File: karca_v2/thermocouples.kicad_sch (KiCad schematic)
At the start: 11 parts, among them J8 Screw_Terminal_01x08, U14 NUP4202, U15 NUP4202, U16 NUP4202, U17 TLV9304xD

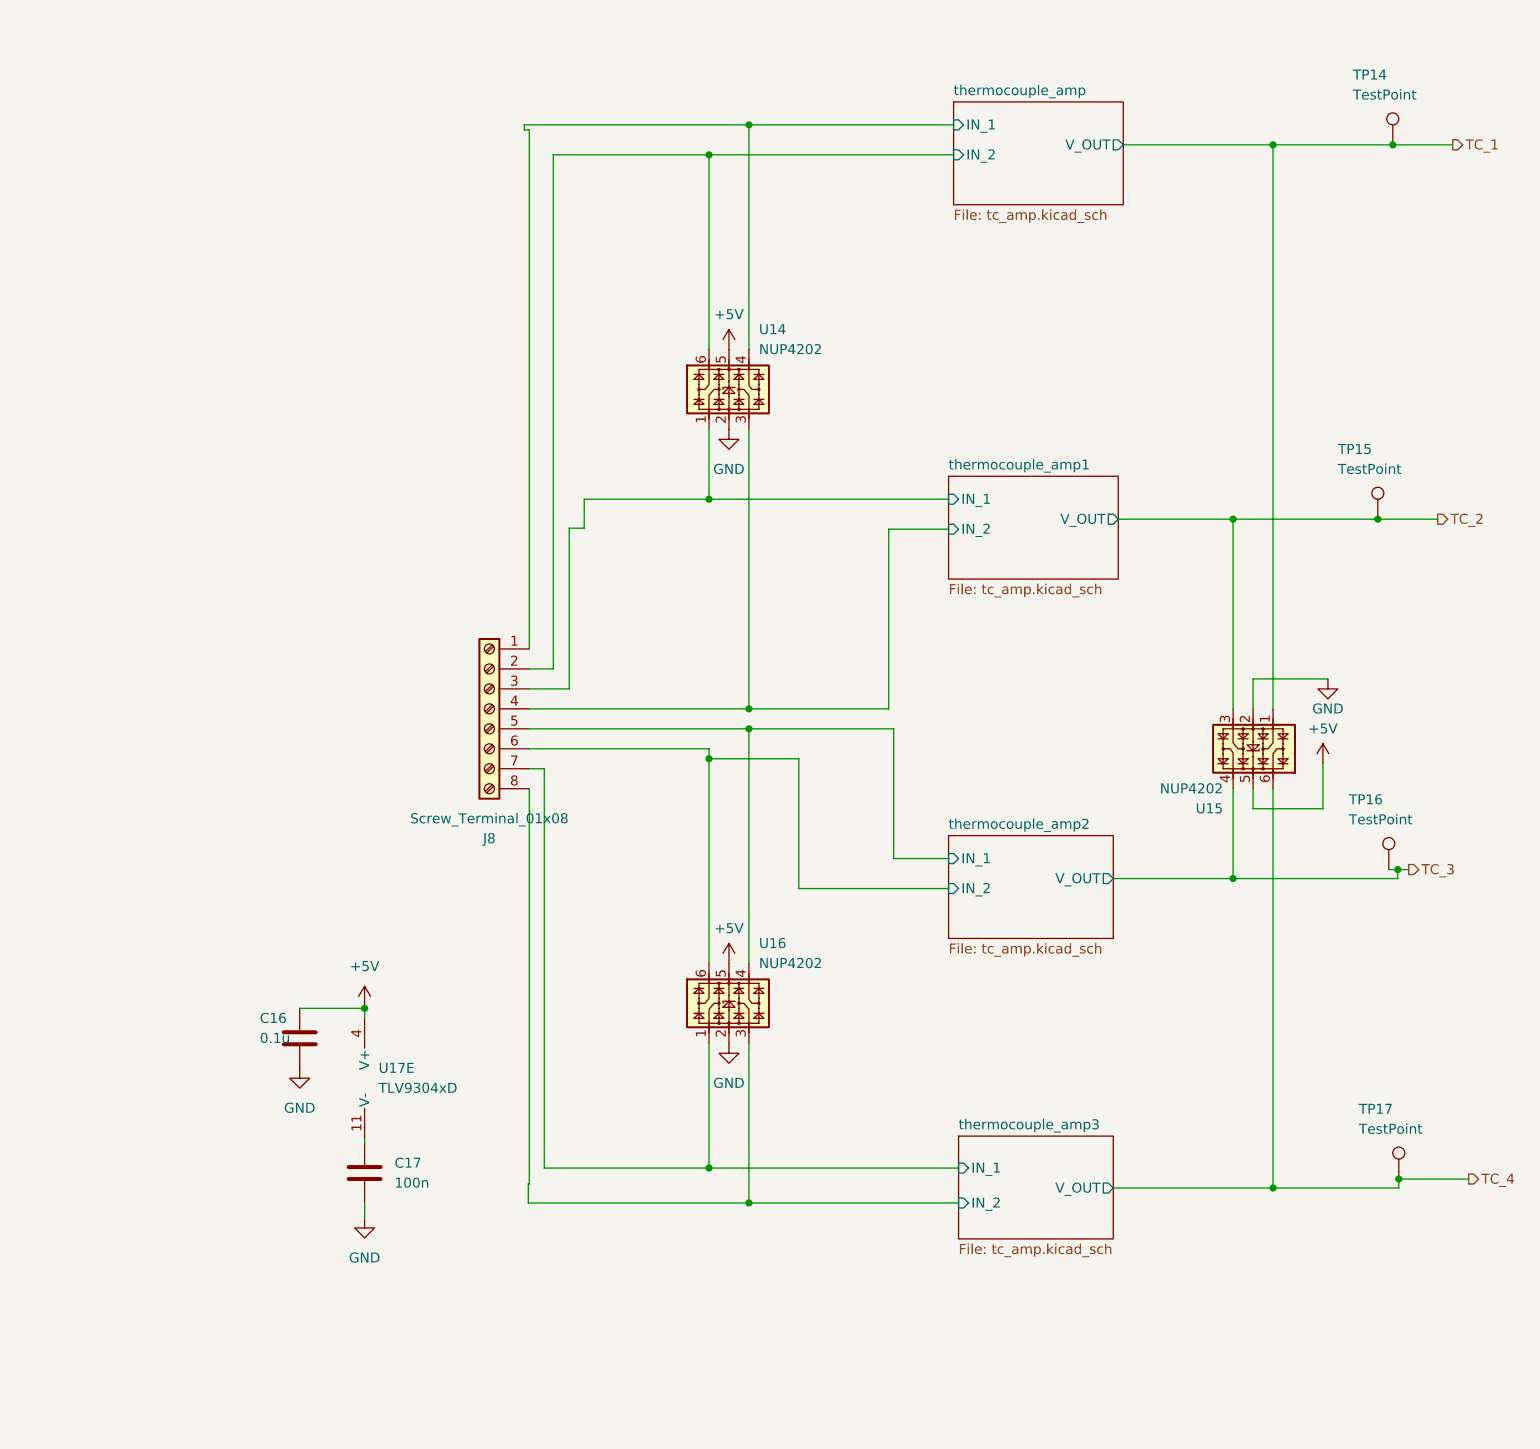
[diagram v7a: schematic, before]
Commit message: cleaned up documentation. Added production files and BOM. Marked Thermocouple components and THT components as DNP (excluded them from BOM too) to match version sent to JLCPCB for fabrication
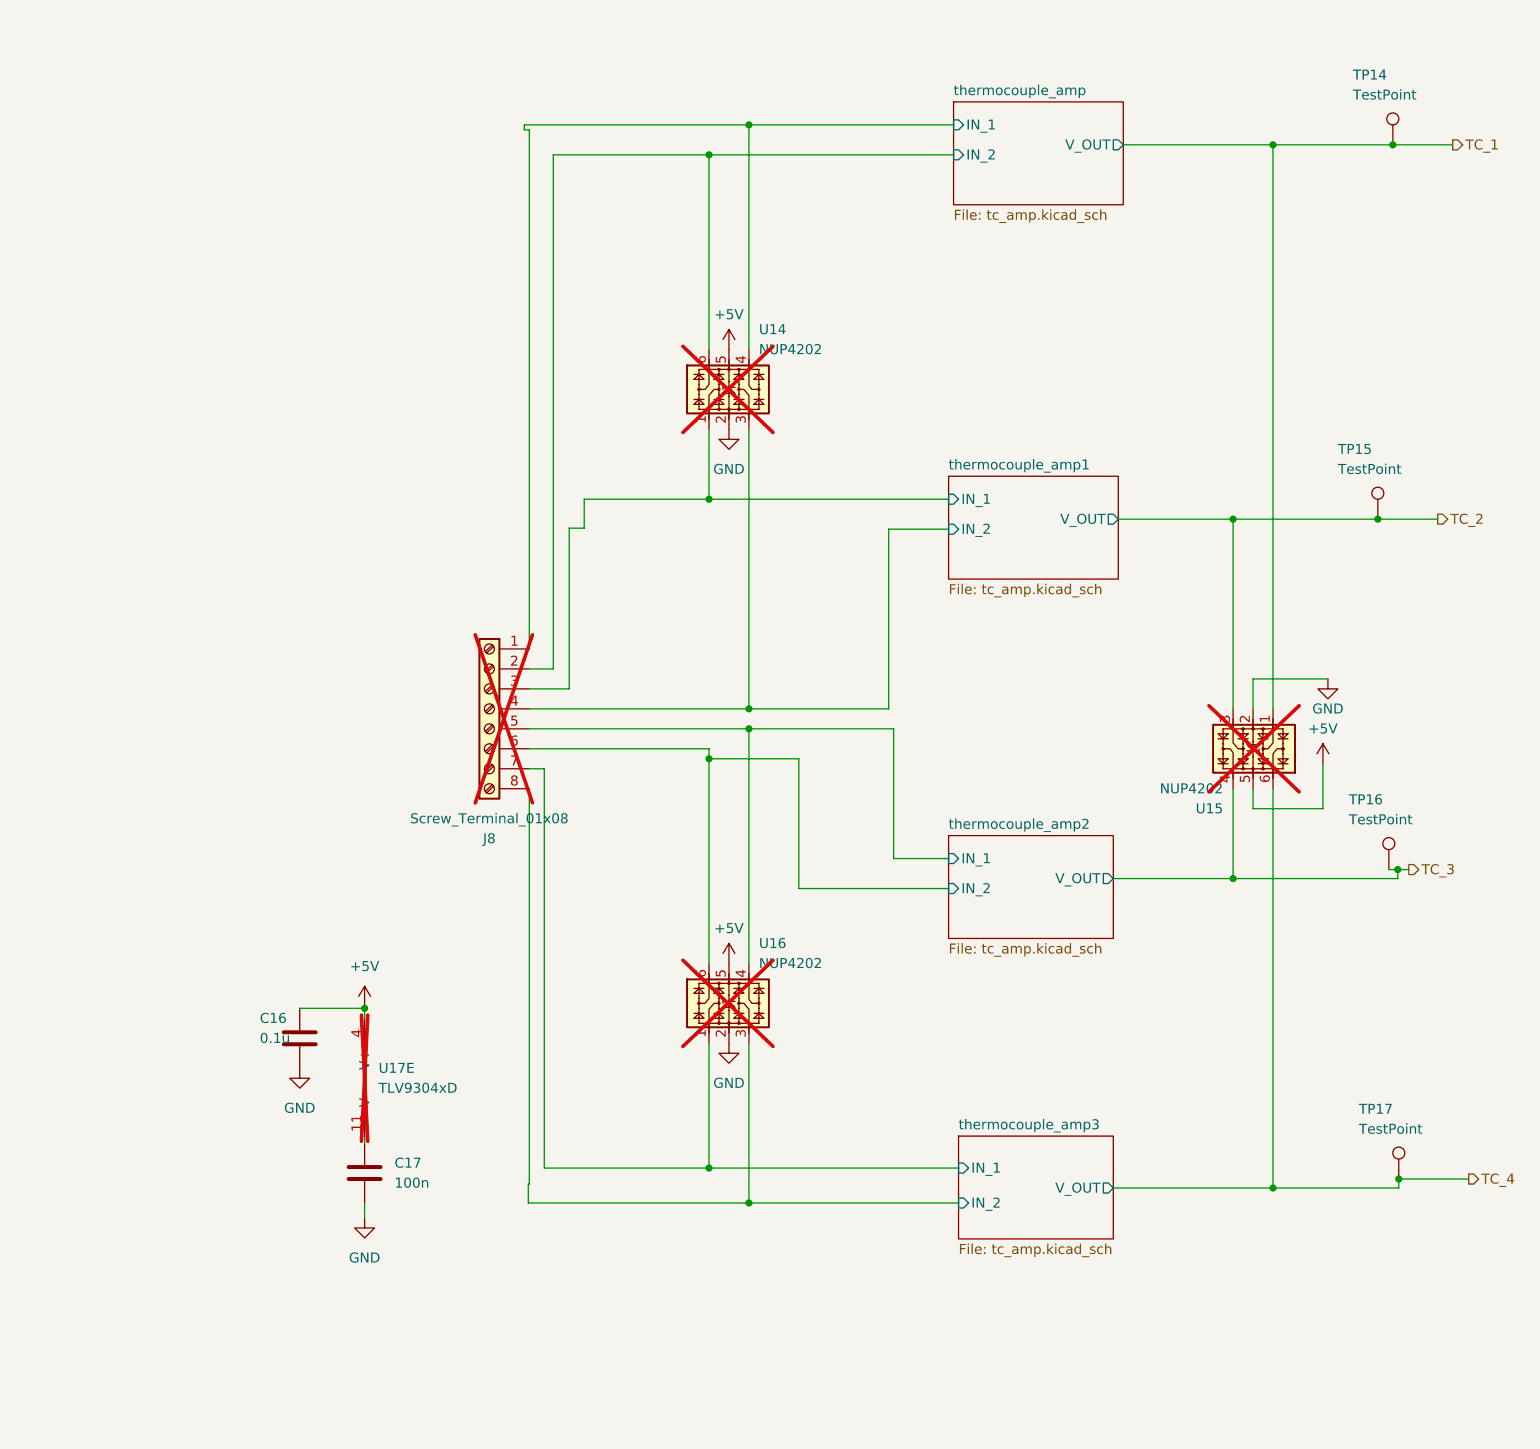
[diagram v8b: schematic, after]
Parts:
- J8, U14, U15, U16, U17: now not fitted; now left out of the parts list
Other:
- company: (none) -> Rice Eclipse
- title: (none) -> kARCA 2.0 Engine Control System
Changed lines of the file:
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@@
 (kicad_sch (version 20230121) (generator eeschema)
   (paper "A4")
+  (title_block
+    (title "kARCA 2.0 Engine Control System")
+    (date "2024-12-16")
+    (rev "1.1")
+    (company "Rice Eclipse")
+    (comment 1 "Designed by Deepak Narayan")
+    (comment 2 "Engine Control System for the Static Engine Testing of Rice Eclipse's Hybrid Rocket Motors")
+  )
   (junction (at 171.45 122.555) (diameter 0) (color 0 0 0 0)
   )
@@
   (symbol (lib_id "power:+5V") (at 107.315 133.35 0) (unit 1)
     (in_bom yes) (on_board yes) (dnp no) (fields_autoplaced)
-    (property "Reference" "#PWR061" (at 107.315 137.16 0)
+    (property "Reference" "#PWR062" (at 107.315 137.16 0)
       (effects (font (size 1.27 1.27)) hide)
     )
@@
       (project "karca_v2"
         (path "/29cf4797-56f2-4f57-ae95-7df639362e3c/4e6489a2-f37d-4c34-b99f-d7711dd1a6f1"
+          (reference "#PWR062") (unit 1)
+        )
+      )
+    )
+  )
+  (symbol (lib_id "power:+5V") (at 182.88 107.95 0) (unit 1)
+    (in_bom yes) (on_board yes) (dnp no) (fields_autoplaced)
+    (property "Reference" "#PWR061" (at 182.88 111.76 0)
+      (effects (font (size 1.27 1.27)) hide)
+    )
+    (property "Value" "+5V" (at 182.88 103.505 0)
+      (effects (font (size 1.27 1.27)))
+    )
+    (property "Footprint" "" (at 182.88 107.95 0)
+      (effects (font (size 1.27 1.27)) hide)
+    )
+    (property "Datasheet" "" (at 182.88 107.95 0)
+      (effects (font (size 1.27 1.27)) hide)
+    )
+    (pin "1")
+    (instances
+      (project "karca_v2"
+        (path "/29cf4797-56f2-4f57-ae95-7df639362e3c/4e6489a2-f37d-4c34-b99f-d7711dd1a6f1"
           (reference "#PWR061") (unit 1)
         )
@@
     )
   )
-  (symbol (lib_id "power:+5V") (at 182.88 107.95 0) (unit 1)
-    (in_bom yes) (on_board yes) (dnp no) (fields_autoplaced)
-    (property "Reference" "#PWR060" (at 182.88 111.76 0)
-      (effects (font (size 1.27 1.27)) hide)
-    )
-    (property "Value" "+5V" (at 182.88 103.505 0)
-      (effects (font (size 1.27 1.27)))
-    )
-    (property "Footprint" "" (at 182.88 107.95 0)
-      (effects (font (size 1.27 1.27)) hide)
-    )
-    (property "Datasheet" "" (at 182.88 107.95 0)
-      (effects (font (size 1.27 1.27)) hide)
-    )
-    (pin "1")
-    (instances
-      (project "karca_v2"
-        (path "/29cf4797-56f2-4f57-ae95-7df639362e3c/4e6489a2-f37d-4c34-b99f-d7711dd1a6f1"
-          (reference "#PWR060") (unit 1)
-        )
-      )
-    )
-  )
   (symbol (lib_id "power:GND") (at 60.96 165.735 0) (unit 1)
     (in_bom yes) (on_board yes) (dnp no) (fields_autoplaced)
-    (property "Reference" "#PWR065" (at 60.96 172.085 0)
+    (property "Reference" "#PWR066" (at 60.96 172.085 0)
       (effects (font (size 1.27 1.27)) hide)
     )
@@
       (project "karca_v2"
         (path "/29cf4797-56f2-4f57-ae95-7df639362e3c/4e6489a2-f37d-4c34-b99f-d7711dd1a6f1"
-          (reference "#PWR065") (unit 1)
+          (reference "#PWR066") (unit 1)
         )
       )
@@
   )
   (symbol (lib_id "Amplifier_Operational:TLV9304xD") (at 63.5 147.955 0) (unit 5)
-    (in_bom yes) (on_board yes) (dnp no) (fields_autoplaced)
+    (in_bom no) (on_board yes) (dnp yes) (fields_autoplaced)
     (property "Reference" "U17" (at 62.738 146.685 0)
       (effects (font (size 1.27 1.27)) (justify left))
@@
   )
   (symbol (lib_id "Power_Protection:NUP4202") (at 107.315 60.325 0) (unit 1)
-    (in_bom yes) (on_board yes) (dnp no)
+    (in_bom no) (on_board yes) (dnp yes)
     (property "Reference" "U14" (at 111.125 52.705 0)
       (effects (font (size 1.27 1.27)) (justify left))
@@
   (symbol (lib_id "power:+5V") (at 60.96 138.811 0) (unit 1)
     (in_bom yes) (on_board yes) (dnp no) (fields_autoplaced)
-    (property "Reference" "#PWR062" (at 60.96 142.621 0)
+    (property "Reference" "#PWR063" (at 60.96 142.621 0)
       (effects (font (size 1.27 1.27)) hide)
     )
@@
       (project "karca_v2"
         (path "/29cf4797-56f2-4f57-ae95-7df639362e3c/4e6489a2-f37d-4c34-b99f-d7711dd1a6f1"
-          (reference "#PWR062") (unit 1)
+          (reference "#PWR063") (unit 1)
         )
       )
@@
   (symbol (lib_id "power:GND") (at 107.315 143.51 0) (unit 1)
     (in_bom yes) (on_board yes) (dnp no) (fields_autoplaced)
-    (property "Reference" "#PWR063" (at 107.315 149.86 0)
+    (property "Reference" "#PWR064" (at 107.315 149.86 0)
       (effects (font (size 1.27 1.27)) hide)
     )
@@
       (project "karca_v2"
         (path "/29cf4797-56f2-4f57-ae95-7df639362e3c/4e6489a2-f37d-4c34-b99f-d7711dd1a6f1"
-          (reference "#PWR063") (unit 1)
+          (reference "#PWR064") (unit 1)
         )
       )
@@
   )
   (symbol (lib_id "Power_Protection:NUP4202") (at 107.315 138.43 0) (unit 1)
-    (in_bom yes) (on_board yes) (dnp no)
+    (in_bom no) (on_board yes) (dnp yes)
     (property "Reference" "U16" (at 111.125 130.81 0)
       (effects (font (size 1.27 1.27)) (justify left))
@@
   )
   (symbol (lib_id "Power_Protection:NUP4202") (at 173.99 106.045 180) (unit 1)
-    (in_bom yes) (on_board yes) (dnp no)
+    (in_bom no) (on_board yes) (dnp yes)
     (property "Reference" "U15" (at 170.18 113.665 0)
       (effects (font (size 1.27 1.27)) (justify left))
@@
   (symbol (lib_id "power:GND") (at 183.515 97.155 0) (unit 1)
     (in_bom yes) (on_board yes) (dnp no)
-    (property "Reference" "#PWR059" (at 183.515 103.505 0)
+    (property "Reference" "#PWR060" (at 183.515 103.505 0)
       (effects (font (size 1.27 1.27)) hide)
     )
@@
       (project "karca_v2"
         (path "/29cf4797-56f2-4f57-ae95-7df639362e3c/4e6489a2-f37d-4c34-b99f-d7711dd1a6f1"
-          (reference "#PWR059") (unit 1)
+          (reference "#PWR060") (unit 1)
         )
       )
@@
   (symbol (lib_id "power:+5V") (at 107.315 55.245 0) (unit 1)
     (in_bom yes) (on_board yes) (dnp no) (fields_autoplaced)
-    (property "Reference" "#PWR057" (at 107.315 59.055 0)
+    (property "Reference" "#PWR058" (at 107.315 59.055 0)
       (effects (font (size 1.27 1.27)) hide)
     )
@@
       (project "karca_v2"
         (path "/29cf4797-56f2-4f57-ae95-7df639362e3c/4e6489a2-f37d-4c34-b99f-d7711dd1a6f1"
-          (reference "#PWR057") (unit 1)
+          (reference "#PWR058") (unit 1)
         )
       )
@@
   (symbol (lib_id "power:GND") (at 107.315 65.405 0) (unit 1)
     (in_bom yes) (on_board yes) (dnp no) (fields_autoplaced)
-    (property "Reference" "#PWR058" (at 107.315 71.755 0)
+    (property "Reference" "#PWR059" (at 107.315 71.755 0)
       (effects (font (size 1.27 1.27)) hide)
     )
@@
       (project "karca_v2"
         (path "/29cf4797-56f2-4f57-ae95-7df639362e3c/4e6489a2-f37d-4c34-b99f-d7711dd1a6f1"
-          (reference "#PWR058") (unit 1)
+          (reference "#PWR059") (unit 1)
         )
       )
@@
   )
   (symbol (lib_id "Connector:Screw_Terminal_01x08") (at 76.835 100.965 0) (mirror y) (unit 1)
-    (in_bom yes) (on_board yes) (dnp no)
+    (in_bom no) (on_board yes) (dnp yes)
     (property "Reference" "J8" (at 76.835 117.475 0)
       (effects (font (size 1.27 1.27)))
@@
   (symbol (lib_id "power:GND") (at 52.705 146.685 0) (unit 1)
     (in_bom yes) (on_board yes) (dnp no) (fields_autoplaced)
-    (property "Reference" "#PWR064" (at 52.705 153.035 0)
+    (property "Reference" "#PWR065" (at 52.705 153.035 0)
       (effects (font (size 1.27 1.27)) hide)
     )
@@
       (project "karca_v2"
         (path "/29cf4797-56f2-4f57-ae95-7df639362e3c/4e6489a2-f37d-4c34-b99f-d7711dd1a6f1"
-          (reference "#PWR064") (unit 1)
-        )
-      )
+          (reference "#PWR065") (unit 1)
+        )
+      )
